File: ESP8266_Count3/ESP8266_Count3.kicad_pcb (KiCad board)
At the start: 2 copper layers, 58.5 x 29.5 mm, 18 parts, among them J2 String1, J3 OLED, SW1 Test, U1 74AHCT1G125, U2 WeMos_D1_mini, U3 AMS1117-5.0, U4 INA219BxD

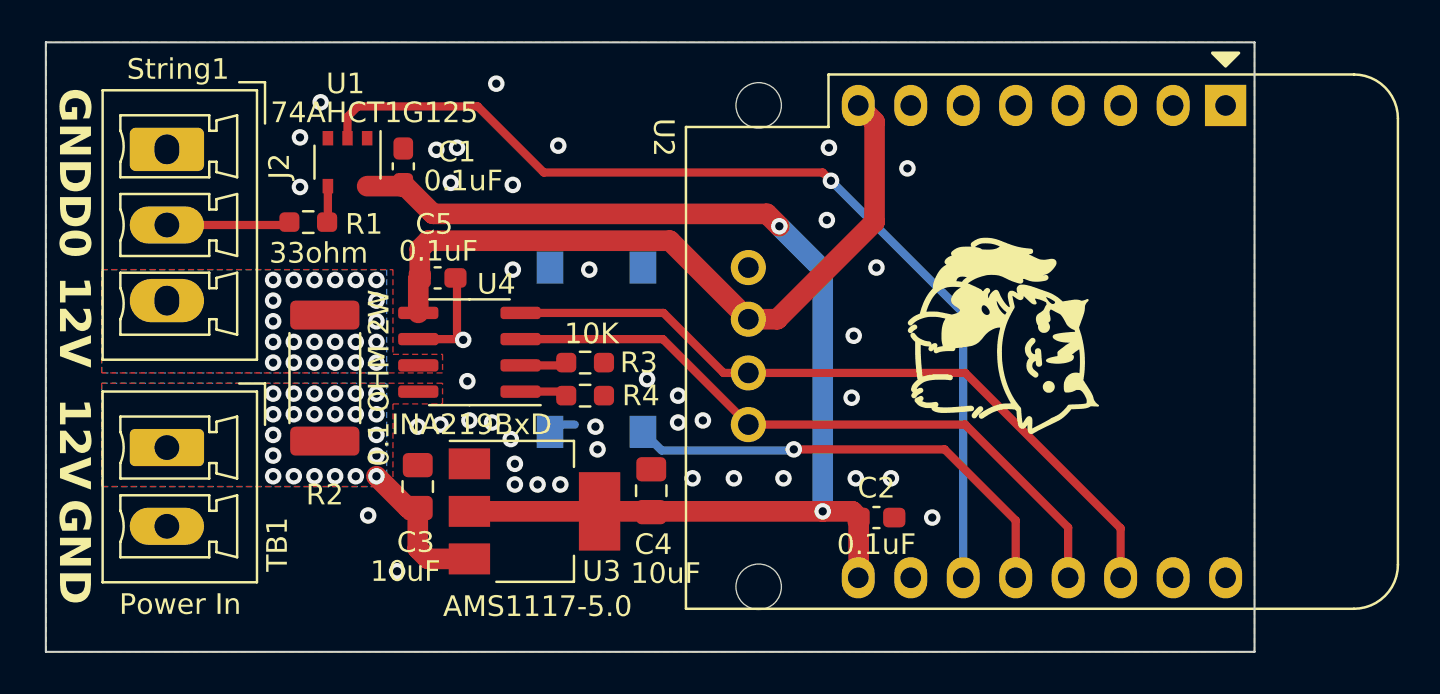
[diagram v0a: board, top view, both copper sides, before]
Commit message: switch to RP2040
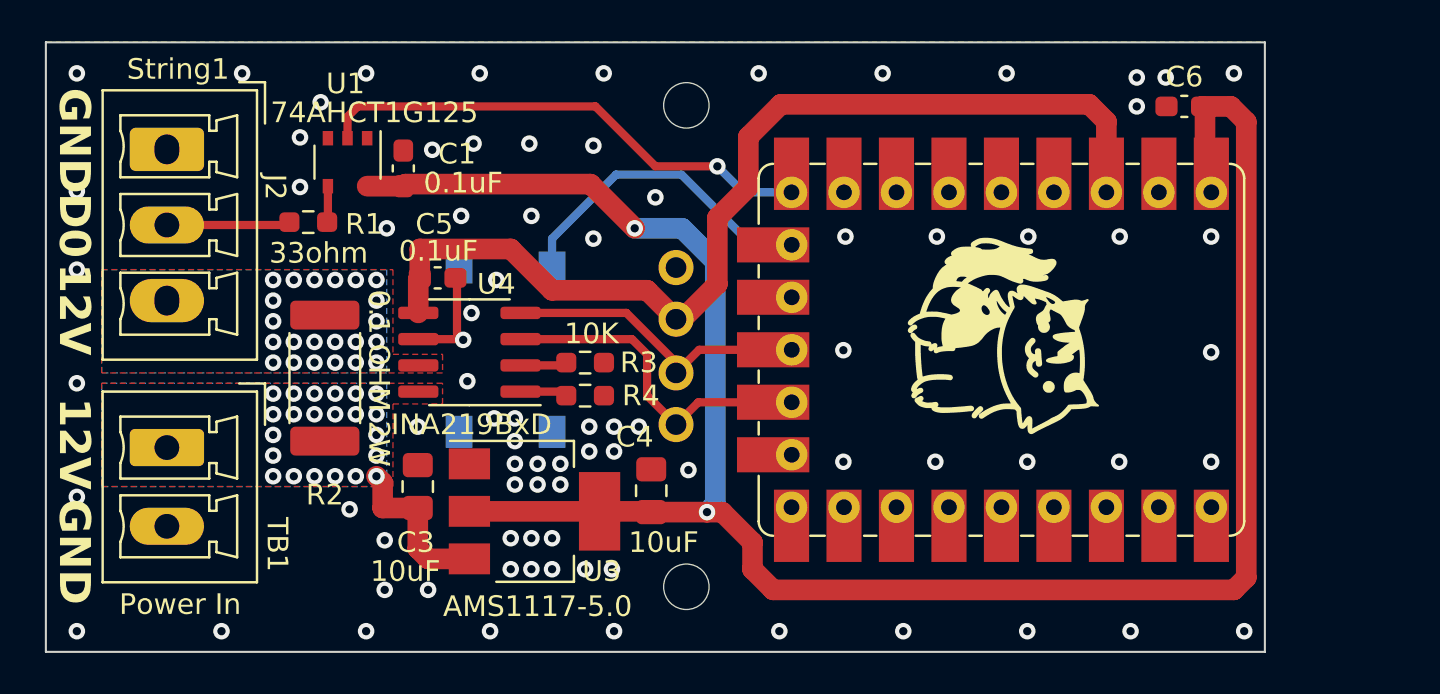
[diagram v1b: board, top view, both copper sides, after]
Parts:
- removed C2: 0.1uF, Capacitor_SMD:C_0603_1608Metric_Pad1.08x0.95mm_HandSolder
- removed U2: WeMos_D1_mini, Module:WEMOS_D1_mini_light
- added C6: 0.1uF, Capacitor_SMD:C_0603_1608Metric_Pad1.08x0.95mm_HandSolder, F.Cu at (154.6, 75.6)
- added U5: RP2040-Tiny, Scotts:RP2040-Tiny_Scott, F.Cu at (157.5, 78.4)
- moved SW1 4.40 mm to (121.8, 87.4)
- moved J3 3.50 mm to (130.0, 87.2)
- moved C1 0.10 mm to (116.8, 78.6)
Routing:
- net +5V: track 57.4 -> 99.8 mm
- net OUT1: track 48.0 -> 24.5 mm
- net I2C_SCL: track 35.8 -> 15.1 mm
- net I2C_SDA: track 32.7 -> 16.5 mm
- net +3.3V: track 34.8 -> 49.1 mm
- net SW1: track 22.6 -> 16.2 mm, vias 1 -> 0
- net GND: track 6.71 -> 5.34 mm, vias 42 -> 82
- net VIN1: track 7.31 -> 8.03 mm
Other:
- board size 58.5 x 29.5 mm -> 59 x 29.5 mm
- board text added: "${TITLE} ${REVISION}"
